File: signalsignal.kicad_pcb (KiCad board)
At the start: 2 copper layers, 49.5 x 49.5 mm, 30 parts, among them IC1 ATTINY841-SSU, P1 CONN_01X32, U1 MCP23S17, U2 MCP23S17, U3 TLC59281, U4 SNx5176, U5 TLC59281

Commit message: v1
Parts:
- removed RA1, RA11, RA13, RA15, RA3, RA5, RA7, RA9: 8K×4, local:TC164
- removed RA10, RA12, RA14, RA16, RA2, RA4, RA6, RA8: 2K×4, local:TC164
- added C10: 0.1µF, local:SMD-0805, F.Cu at (139.1, 126.4)
- added C2: 0.1µF, local:SMD-0805, F.Cu at (112.4, 118.1)
- added C7: C, local:SMD-0805, F.Cu at (128.3, 134.6)
- added C8: C, local:SMD-0805, F.Cu at (124.5, 134.6)
- added C9: 0.33µF, local:SMD-0805, F.Cu at (139.1, 122.6)
- added P2: CONN_01X32, local:Pin_Header_Straight_2x16, F.Cu at (125.1, 146.1)
- added P3: ISP, local:Pin_Header_Straight_2x03, F.Cu at (123.8, 115.6)
- added P4: CONN_01X04, local:RT063xxHBWC, F.Cu at (104.1, 125.1)
- added P5: CONN_01X04, local:RT063xxHBWC, F.Cu at (146.1, 125.1)
- added R3: R, local:SMD-0805, F.Cu at (140.3, 134.0)
- added R4: R, local:SMD-0805, F.Cu at (120.0, 134.0)
- added U6: 7805, local:SOT89-3, F.Cu at (134.6, 125.1)
- added X1: CRYSTAL, local:Crystal_HC49-U_Vertical, F.Cu at (127.0, 130.8)
- C1, C3, C4, C5, C6, R1, R2: footprint SMD_Packages:SMD-0805 -> local:SMD-0805
- IC1: footprint SMD_Packages:SOIC-14_N -> local:SOIC-14_N
- P1: footprint Pin_Headers:Pin_Header_Straight_2x16 -> local:Pin_Header_Straight_2x16
- U1, U2: value MCP23S17 -> TLC5928; footprint SMD_Packages:SSOP-28 -> local:SSOP-24
- U3: value TLC59281 -> TLC5928; footprint SMD_Packages:SSOP-24 -> local:SSOP-24
- U4: value SNx5176 -> TLC5928; footprint SMD_Packages:SOIC-8-N -> local:SSOP-24
- U5: value TLC59281 -> SNx5176; footprint SMD_Packages:SSOP-24 -> local:SOIC-8-N
- moved C5 38.0 mm to (112.4, 130.2)
- moved R1 27.7 mm to (130.2, 116.2), turned to 270 degrees
- moved R2 26.3 mm to (109.9, 116.2)
- moved IC1 26.0 mm to (125.1, 123.2), turned to 90 degrees
- moved U3 22.7 mm to (135.3, 138.4), turned to 270 degrees
- moved U1 21.5 mm to (135.3, 111.8)
- moved U2 19.5 mm to (114.9, 111.8)
- moved P1 18.8 mm to (125.1, 104.1)
- moved U5 17.9 mm to (116.8, 126.4)
- moved C6 16.2 mm to (130.2, 125.7), turned to 90 degrees
- moved C1 14.9 mm to (132.7, 118.1), turned to 270 degrees
- moved C3 8.99 mm to (137.8, 132.1), turned to 90 degrees
- moved U4 6.02 mm to (114.9, 138.4)
- moved C4 5.85 mm to (117.5, 132.1), turned to 90 degrees
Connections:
- IC1 pad 10: /CS_INPUT -> /BLANK
- IC1 pad 2: (no net) -> Net-(C7-Pad2)
- IC1 pad 3: (no net) -> Net-(C8-Pad2)
- IC1 pad 4: (no net) -> /RESET
- IC1 pad 5: /INT -> (no net)
- U1 pad 1: /l11 -> GND
- U1 pad 10: GND -> /p27
- U1 pad 11: /CS_INPUT -> /p25
- U1 pad 12: /SCK -> /p26
- U1 pad 13: /MOSI -> /p22
- U1 pad 14: /MISO -> /p23
- U1 pad 15: GND -> /p24
- U1 pad 16: GND -> /p21
- U1 pad 17: GND -> /p20
- U1 pad 18: +5V -> /p19
- U1 pad 19: (no net) -> /p18
- U1 pad 2: /l10 -> /MOSI
- U1 pad 20: /INT -> /p17
- U1 pad 21: /l1 -> /BLANK
- U1 pad 22: /l2 -> Net-(U1-Pad22)
- U1 pad 23: /l3 -> Net-(R1-Pad1)
- U1 pad 24: /l4 -> +5V
- U1 pad 3: /l9 -> /SCK
- U1 pad 4: /l12 -> /LATCH
- U1 pad 5: /l13 -> /p32
- U1 pad 6: /l14 -> /p31
- U1 pad 7: /l15 -> /p30
- U1 pad 8: /l16 -> /p29
- U1 pad 9: +5V -> /p28
- U2 pad 1: /l27 -> GND
- U2 pad 10: GND -> /p11
- U2 pad 11: /CS_INPUT -> /p9
- U2 pad 12: /SCK -> /p10
- U2 pad 13: /MOSI -> /p6
- U2 pad 14: /MISO -> /p7
- U2 pad 15: GND -> /p8
- U2 pad 16: GND -> /p5
- U2 pad 17: +5V -> /p4
- U2 pad 18: +5V -> /p3
- U2 pad 19: (no net) -> /p2
- U2 pad 2: /l26 -> Net-(U1-Pad22)
- U2 pad 20: /INT -> /p1
- U2 pad 21: /l17 -> /BLANK
- U2 pad 22: /l18 -> Net-(U2-Pad22)
- U2 pad 23: /l19 -> Net-(R2-Pad1)
- U2 pad 24: /l20 -> +5V
- U2 pad 3: /l25 -> /SCK
- U2 pad 4: /l28 -> /LATCH
- U2 pad 5: /l29 -> /p16
- U2 pad 6: /l30 -> /p15
- U2 pad 7: /l31 -> /p14
- U2 pad 8: /l32 -> /p13
- U2 pad 9: +5V -> /p12
- U3 pad 10: /p11 -> /p43
- U3 pad 11: /p9 -> /p41
- U3 pad 12: /p10 -> /p42
- U3 pad 13: /p6 -> /p38
- U3 pad 14: /p7 -> /p39
- U3 pad 15: /p8 -> /p40
- U3 pad 16: /p5 -> /p37
- U3 pad 17: /p4 -> /p36
- U3 pad 18: /p3 -> /p35
- U3 pad 19: /p2 -> /p34
- U3 pad 2: Net-(U3-Pad2) -> Net-(U2-Pad22)
- U3 pad 20: /p1 -> /p33
- U3 pad 21: (no net) -> /BLANK
- U3 pad 22: (no net) -> Net-(U3-Pad22)
- U3 pad 23: Net-(R1-Pad1) -> Net-(R3-Pad1)
- U3 pad 5: /p16 -> /p48
- U3 pad 6: /p15 -> /p47
- U3 pad 7: /p14 -> /p46
- U3 pad 8: /p13 -> /p45
- U3 pad 9: /p12 -> /p44
- U4 pad 1: /RX -> GND
- U4 pad 2: /DIR -> Net-(U3-Pad22)
- U4 pad 3: /DIR -> /SCK
- U4 pad 4: /TX -> /LATCH
- U4 pad 5: GND -> /p64
- U4 pad 6: (no net) -> /p63
- U4 pad 7: (no net) -> /p62
- U4 pad 8: +5V -> /p61
- U5 pad 1: GND -> /RX
- U5 pad 2: /MOSI -> /DIR
- U5 pad 3: /SCK -> /DIR
- U5 pad 4: /LATCH -> /TX
- U5 pad 5: /p32 -> GND
- U5 pad 6: /p31 -> /A
- U5 pad 7: /p30 -> /B
- U5 pad 8: /p29 -> +5V
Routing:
- net /BLANK: track 0.00 -> 133.2 mm, vias 0 -> 4
- net /LATCH: track 24.0 -> 151.1 mm, vias 2 -> 4
- net /CS_INPUT: track 106.7 -> 0.00 mm, vias 2 -> 0
- net /MOSI: track 114.8 -> 23.9 mm
- net +5V: track 26.3 -> 103.2 mm, vias 0 -> 2
- net /INT: track 62.5 -> 0.00 mm, vias 2 -> 0
- net /B: track 0.00 -> 55.1 mm
- net /A: track 0.00 -> 54.7 mm
- net /+17V: track 0.00 -> 54.4 mm
- net GND: track 24.2 -> 63.1 mm, vias 0 -> 26
- net Net-(U2-Pad22): track 0.00 -> 38.6 mm, vias 0 -> 2
- net Net-(U1-Pad22): track 0.00 -> 31.3 mm, vias 0 -> 2
- net Net-(U3-Pad22): track 0.00 -> 29.6 mm, vias 0 -> 2
- net /SCK: track 110.6 -> 134.9 mm, vias 0 -> 2
- net /l17: track 16.0 -> 0.00 mm, vias 1 -> 0
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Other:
- outline, holes or cut-outs redrawn
- net class Default: via_dia 0.889 -> 0.7; via_drill 0.635 -> 0.4
- rule via_min_drill: 0.508 -> 0.3
- rule via_min_size: 0.889 -> 0.5
- board text added: "1-32"
- board text added: "17V"
- board text added: "33-64"
- board text added: "GND"
- board text added: "RS485"

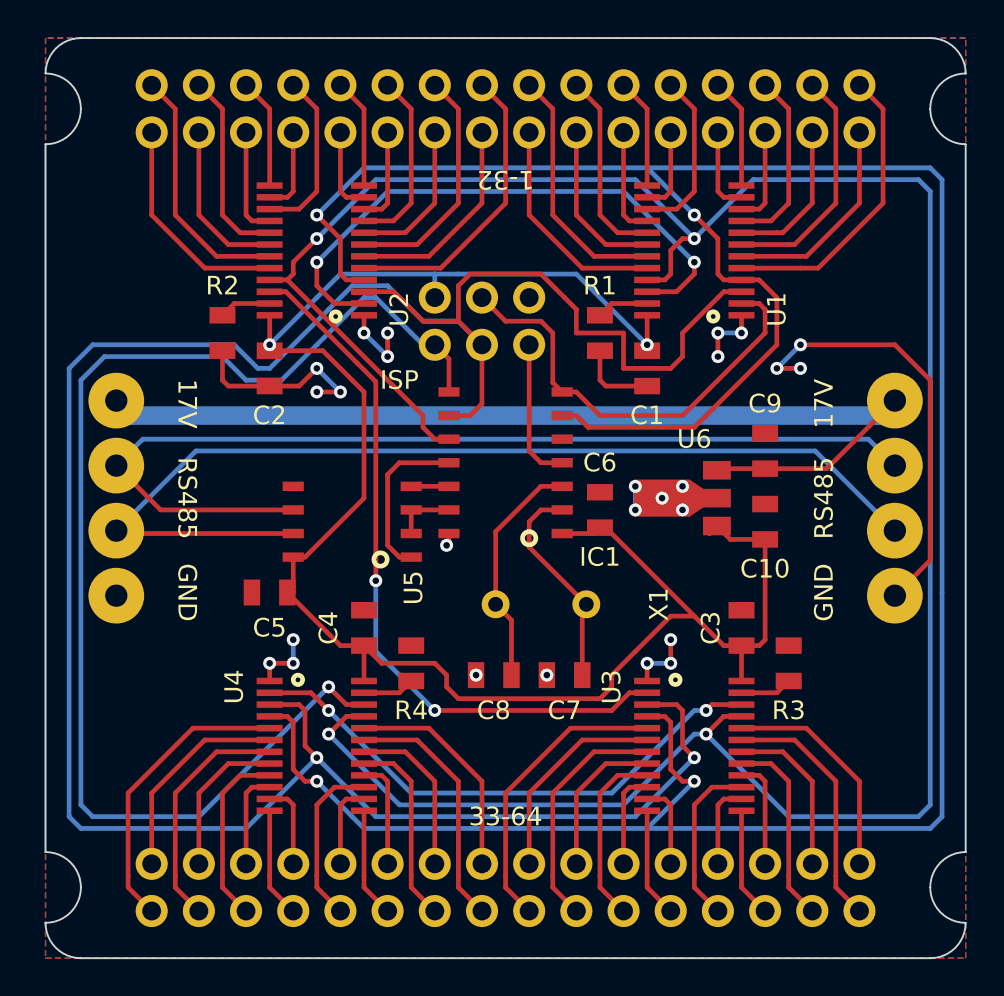
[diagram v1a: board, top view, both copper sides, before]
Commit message: Switched to switcher
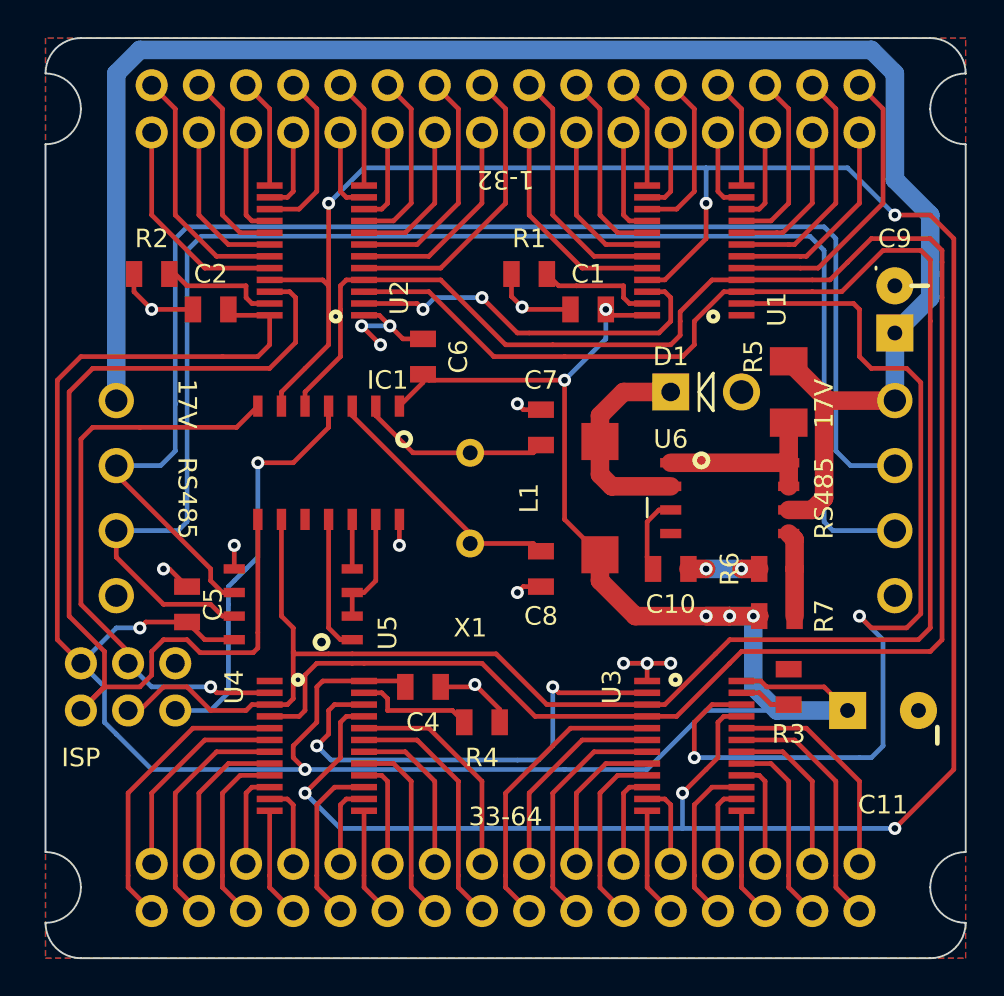
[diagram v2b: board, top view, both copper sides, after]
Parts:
- removed C3: 0.1µF, local:SMD-0805
- added C11: 470µF, local:Capacitor8x13RM3.8, F.Cu at (145.4, 136.5)
- added D1: DIODESCH, Diodes_ThroughHole:Diode_DO-41_SOD81_Vertical_AnodeUp, F.Cu at (134.0, 119.4)
- added L1: 220µH, local:SELF-WE-PD3S, F.Cu at (130.2, 125.1)
- added R5: 0.33, local:SMD-1206, F.Cu at (140.3, 119.4)
- added R6: 1.2k, local:SMD-0805, F.Cu at (139.7, 128.9)
- added R7: 3.8k, local:SMD-0805, F.Cu at (139.7, 131.4)
- C10: value 0.1µF -> 470pF
- C9: value 0.33µF -> 100µF; footprint local:SMD-0805 -> local:Capacitor5x11RM2.5
- U6: value 7805 -> MC34063; footprint local:SOT89-3 -> local:SOIC-8-N
- moved P3 27.4 mm to (104.8, 135.3)
- moved C7 13.4 mm to (127.0, 121.3), turned to 270 degrees
- moved C6 12.6 mm to (120.7, 117.5)
- moved C9 10.3 mm to (146.1, 114.9), turned to 0 degrees
- moved IC1 9.53 mm to (115.6, 123.2), turned to 180 degrees
- moved X1 6.87 mm to (123.2, 125.1), turned to 270 degrees
- moved C8 6.25 mm to (127.0, 128.9), turned to 90 degrees
- moved C10 5.68 mm to (134.0, 128.9), turned to 0 degrees
- moved U5 5.46 mm to (113.7, 130.8)
- moved R1 4.96 mm to (126.4, 113.0), turned to 180 degrees
- moved R2 4.96 mm to (106.0, 113.0), turned to 180 degrees
- moved R4 4.96 mm to (123.8, 137.2), turned to 0 degrees
- moved C1 4.49 mm to (129.5, 114.9), turned to 180 degrees
- moved C2 4.49 mm to (109.2, 114.9), turned to 180 degrees
- moved C4 4.49 mm to (120.7, 135.3), turned to 0 degrees
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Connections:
- C10 pad 1: +5V -> Net-(C10-Pad1)
- IC1 pad 10: /BLANK -> (no net)
- IC1 pad 5: (no net) -> /LATCH
- IC1 pad 6: /LATCH -> /BLANK
- U1 pad 2: /MOSI -> Net-(U1-Pad2)
- U2 pad 22: Net-(U2-Pad22) -> /MISO
- U3 pad 2: Net-(U2-Pad22) -> Net-(U3-Pad2)
- U3 pad 22: Net-(U3-Pad22) -> Net-(U1-Pad2)
- U4 pad 2: Net-(U3-Pad22) -> /MOSI
- U4 pad 22: /MISO -> Net-(U3-Pad2)
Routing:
- net +5V: track 103.2 -> 155.8 mm, vias 2 -> 7
- net Net-(U1-Pad2): track 0.00 -> 52.0 mm, vias 0 -> 2
- net /LATCH: track 151.1 -> 106.9 mm, vias 4 -> 0
- net /+17V: track 54.4 -> 95.6 mm
- net Net-(U2-Pad22): track 38.6 -> 0.00 mm, vias 2 -> 0
- net Net-(U3-Pad22): track 29.6 -> 0.00 mm, vias 2 -> 0
- net GND: track 63.1 -> 36.4 mm, vias 26 -> 16
- net /B: track 55.1 -> 81.6 mm
- net Net-(U3-Pad2): track 0.00 -> 25.9 mm, vias 0 -> 2
- net /SCK: track 134.9 -> 112.4 mm, vias 2 -> 0
- net /A: track 54.7 -> 75.9 mm
- net /RESET: track 7.76 -> 23.2 mm, vias 0 -> 1
- net /MISO: track 67.5 -> 54.9 mm, vias 1 -> 0
- net Net-(D1-Pad2): track 0.00 -> 11.8 mm
- net Net-(U1-Pad22): track 31.3 -> 20.6 mm
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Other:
- board text removed: "GND"

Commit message: tidy
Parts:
- moved C11 0.63 mm to (145.4, 137.2), turned to 180 degrees
- moved R3 0.23 mm to (140.2, 135.4)
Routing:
- net GND: track 36.4 -> 134.0 mm, vias 16 -> 25
- net Net-(U1-Pad2): track 52.0 -> 47.5 mm
- net /MOSI: track 31.7 -> 34.7 mm
- net Net-(U3-Pad2): track 25.9 -> 23.4 mm
- net Net-(C7-Pad2): track 10.4 -> 12.6 mm
- net /LATCH: track 106.9 -> 108.3 mm
- net /B: track 81.6 -> 80.4 mm
- net Net-(C8-Pad2): track 14.0 -> 15.1 mm
- net +5V: track 155.8 -> 156.7 mm
- net /A: track 75.9 -> 75.3 mm
- net /SCK: track 112.4 -> 113.0 mm
- net /BLANK: track 138.7 -> 139.2 mm, vias 6 -> 4
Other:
- board text added: "V0.1"
- board text added: "©2015 b@Zi.iS CC BY-SA"
